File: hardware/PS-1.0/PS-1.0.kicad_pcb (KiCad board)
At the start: 2 copper layers, 98.4 x 199.4 mm, 50 parts, among them J5 Conn_01x04, J8 Conn_01x03, J9 Conn_01x03, K1 RAYEX-L90, K2 RAYEX-L90, Q1 IRFPE50, Q2 IRFPE50, Q3 IRFPE50, U1 TC4422

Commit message: deleted:    hardware/MSD-1.0/MSD-1.0-backups/MSD-1.0-2025-03-24_113503.zip 	new file:   hardware/MSD-1.0/MSD-1.0-backups/MSD-1.0-2025-04-14_090414.zip 	new file:   hardware/MSD-2.0/MSD-2.0-backups/MSD-2.0-2025-04-14_085637.zip 	deleted:    hardware/PS-1.0/PS-1.0-backups/PS-1.0-2025-04-11_100523.zip 	new file:   hardware/PS-1.0/PS-1.0-backups/PS-1.0-2025-04-14_085622.zip 	modified:   hardware/PS-1.0/PS-1.0.kicad_pcb 	deleted:    hardware/PS-1.0/_autosave-PS-1.0.kicad_pcb 	renamed:    hardware/PS-1.0/~PS-1.0.kicad_sch.lck -> hardware/REM-3.0/~REM-3.0.kicad_pcb.lck 	renamed:    hardware/PS-1.0/~_autosave-PS-1.0.kicad_pcb.lck -> hardware/REM-3.0/~REM-3.0.kicad_sch.lck 	modified:   pic/.DS_Store 	new file:   pic/REM/REM XF.png 	new file:   pic/REM/REM-1kohm.png 	new file:   pic/REM/REM-200ohm.png 	new file:   pic/REM/REM-5ohm.png 	new file:   pic/REM/REM-highZ.png
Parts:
- U3: footprint Custom:ESU-REM-3.0 -> Custom:ESU-MSD-1.0
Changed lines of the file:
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@@
 		)
 	)
-	(footprint "Custom:ESU-REM-3.0"
+	(footprint "Custom:ESU-MSD-1.0"
 		(layer "F.Cu")
 		(at 134.62 130.175)
@@
 			)
 		)
-		(property "Footprint" "Custom:ESU-REM-3.0"
+		(property "Footprint" "Custom:ESU-MSD-1.0"
 			(at -9.525 4.1275 0)
 			(unlocked yes)
@@
 			(remove_unused_layers no)
 		)
-		(model "${KIPRJMOD}/REM-3.0.step"
+		(model "/Users/margabudi/Documents/hardware/ESU/hardware/MSD-1.0/MSD-1.0.step"
 			(offset
 				(xyz 1.6 0 0)

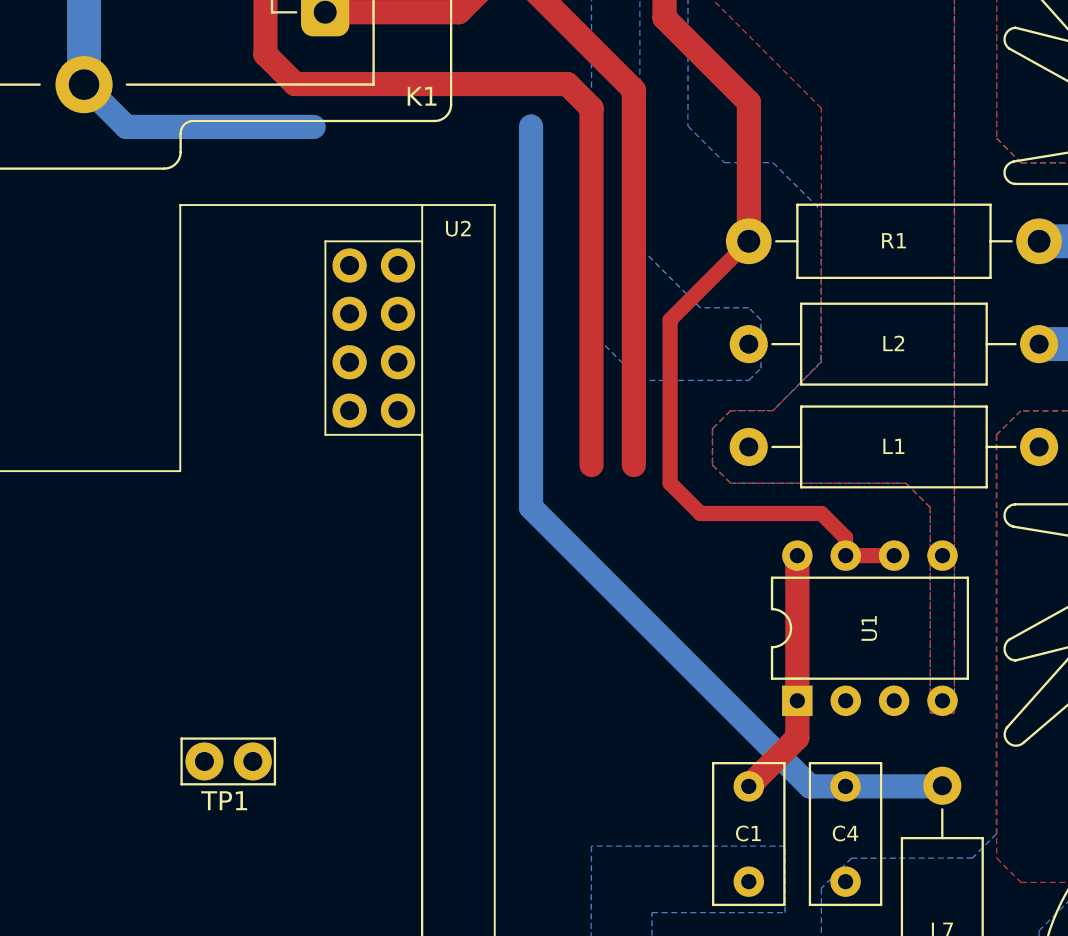
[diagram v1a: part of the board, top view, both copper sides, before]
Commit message: new file:   hardware/Gain/Gain-B_Cu.gbr 	new file:   hardware/Gain/Gain-B_Mask.gbr 	new file:   hardware/Gain/Gain-B_Paste.gbr 	new file:   hardware/Gain/Gain-B_Silkscreen.gbr 	new file:   hardware/Gain/Gain-Edge_Cuts.gbr 	new file:   hardware/Gain/Gain-F_Cu.gbr 	new file:   hardware/Gain/Gain-F_Mask.gbr 	new file:   hardware/Gain/Gain-F_Paste.gbr 	new file:   hardware/Gain/Gain-F_Silkscreen.gbr 	new file:   hardware/Gain/Gain-NPTH.drl 	new file:   hardware/Gain/Gain-PTH.drl 	new file:   hardware/Gain/Gain-backups/Gain-2025-04-14_115147.zip 	new file:   hardware/Gain/Gain-backups/Gain-2025-04-14_121847.zip 	new file:   hardware/Gain/Gain-backups/Gain-2025-04-14_133755.zip 	new file:   hardware/Gain/Gain-backups/Gain-2025-04-14_141907.zip 	new file:   hardware/Gain/Gain-backups/Gain-2025-04-14_162042.zip 	new file:   hardware/Gain/Gain-backups/Gain-2025-04-14_163456.zip 	new file:   hardware/Gain/Gain-job.gbrjob 	new file:   hardware/Gain/Gain.kicad_pcb 	new file:   hardware/Gain/Gain.kicad_prl 	new file:   hardware/Gain/Gain.kicad_pro 	new file:   hardware/Gain/Gain.kicad_sch 	new file:   hardware/Gain/Gain.step 	new file:   hardware/Gain/REM-2.0 BoM.csv 	new file:   hardware/Gain/REM-2.0-backups/REM-2.0-2025-03-05_160217.zip 	new file:   hardware/Gain/REM-2.0-backups/REM-2.0-2025-03-06_081735.zip 	new file:   hardware/Gain/REM-2.0-backups/REM-2.0-2025-03-17_111724.zip 	new file:   hardware/Gain/REM-2.0-backups/REM-2.0-2025-03-17_135033.zip 	new file:   hardware/Gain/REM-2.0-backups/REM-2.0-2025-03-18_104019.zip 	new file:   hardware/Gain/REM-2.0-backups/REM-2.0-2025-03-18_141720.zip 	new file:   hardware/Gain/REM-2.0-backups/REM-2.0-2025-03-18_202240.zip 	new file:   hardware/Gain/REM-2.0-backups/REM-2.0-2025-03-18_203414.zip 	new file:   hardware/Gain/REM-2.0-backups/REM-2.0-2025-03-18_204444.zip 	new file:   hardware/Gain/REM-2.0-backups/REM-2.0-2025-03-24_102406.zip 	new file:   hardware/Gain/REM-2.0-backups/REM-2.0-2025-03-24_103843.zip 	new file:   hardware/Ga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
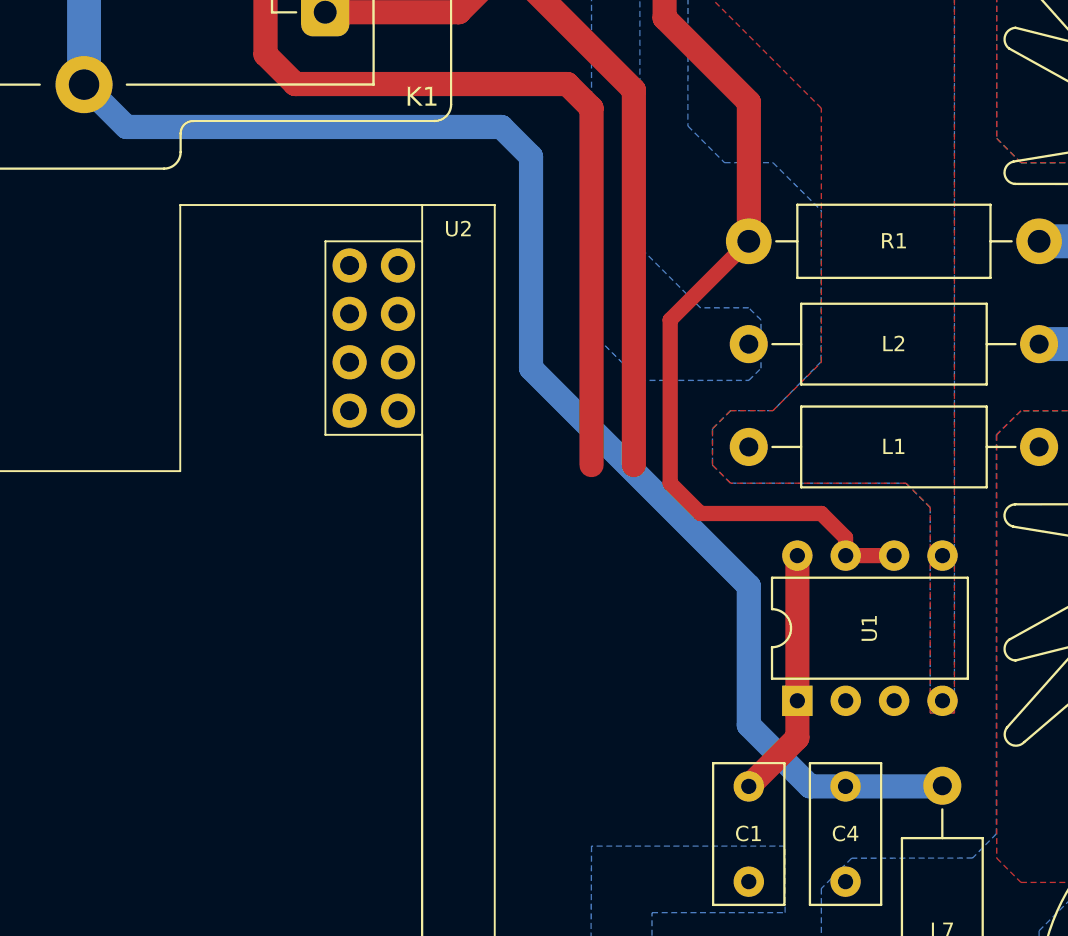
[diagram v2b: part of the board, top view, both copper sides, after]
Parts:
- removed TP1: TestPoint, TestPoint:TestPoint_Bridge_Pitch2.54mm_Drill1.0mm
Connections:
- net Net-(D8-A) renamed /RLY-K
- net Net-(D8-K) renamed /RLY-A
- net Net-(J5-Pin_1) renamed /PWM
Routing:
- net Net-(C4-Pad1): track 110.0 -> 120.4 mm

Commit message: deleted:    hardware/Gain/Gain-backups/Gain-2025-04-14_115147.zip 	new file:   hardware/Gain/Gain-backups/Gain-2025-04-15_120154.zip 	deleted:    hardware/MSD-1.0/MSD-1.0-backups/MSD-1.0-2025-03-24_134332.zip 	deleted:    hardware/MSD-1.0/MSD-1.0-backups/MSD-1.0-2025-03-25_144744.zip 	deleted:    hardware/MSD-1.0/MSD-1.0-backups/MSD-1.0-2025-03-25_145433.zip 	deleted:    hardware/MSD-1.0/MSD-1.0-backups/MSD-1.0-2025-03-25_150210.zip 	deleted:    hardware/MSD-1.0/MSD-1.0-backups/MSD-1.0-2025-03-25_150818.zip 	new file:   hardware/MSD-1.0/MSD-1.0-backups/MSD-1.0-2025-04-16_142822.zip 	new file:   hardware/MSD-1.0/MSD-1.0-backups/MSD-1.0-2025-04-16_143722.zip 	new file:   hardware/MSD-1.0/MSD-1.0-backups/MSD-1.0-2025-04-16_145208.zip 	new file:   hardware/MSD-1.0/MSD-1.0-backups/MSD-1.0-2025-04-16_150237.zip 	new file:   hardware/MSD-1.0/MSD-1.0-backups/MSD-1.0-2025-04-16_150829.zip 	modified:   hardware/MSD-1.0/MSD-1.0.kicad_pcb 	modified:   hardware/MSD-1.0/MSD-1.0.kicad_sch 	modified:   hardware/MSD-1.0/MSD-1.0.step 	new file:   hardware/MSD-2.0/MSD-2.0-backups/MSD-2.0-2025-04-16_090248.zip 	deleted:    hardware/PS-1.0/PS-1.0-backups/PS-1.0-2025-03-18_205016.zip 	deleted:    hardware/PS-1.0/PS-1.0-backups/PS-1.0-2025-03-18_205728.zip 	deleted:    hardware/PS-1.0/PS-1.0-backups/PS-1.0-2025-03-18_211157.zip 	deleted:    hardware/PS-1.0/PS-1.0-backups/PS-1.0-2025-03-18_213933.zip 	deleted:    hardware/PS-1.0/PS-1.0-backups/PS-1.0-2025-03-19_094557.zip 	deleted:    hardware/PS-1.0/PS-1.0-backups/PS-1.0-2025-03-19_101204.zip 	deleted:    hardware/PS-1.0/PS-1.0-backups/PS-1.0-2025-03-19_102323.zip 	new file:   hardware/PS-1.0/PS-1.0-backups/PS-1.0-2025-04-16_154157.zip 	new file:   hardware/PS-1.0/PS-1.0-backups/PS-1.0-2025-04-16_154838.zip 	new file:   hardware/PS-1.0/PS-1.0-backups/PS-1.0-2025-04-16_155906.zip 	new file:   hardware/PS-1.0/PS-1.0-backups/PS-1.0-2025-04-16_160456.zip 	new file:   hardware/PS-1.0/PS-1.0-backups/PS-1.0-2025-04-16_161300.zip 	new file:   har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
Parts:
- removed HS1, HS2, HS3: Heatsink_Pad, Heatsink:Heatsink_Fischer_SK129-STS_42x25mm_2xDrill2.5mm
- removed HS4, HS5: Heatsink_Pad, Heatsink:Heatsink_Stonecold_HS-132_32x14mm_2xFixation1.5mm
- removed J5: Conn_01x04, Connector_PinHeader_2.54mm:PinHeader_1x04_P2.54mm_Vertical
- added J1: Conn_02x16_Odd_Even, Connector_PinSocket_2.54mm:PinSocket_2x16_P2.54mm_Vertical, F.Cu at (182.2, 186.7)
- added J2: Conn_01x05, Connector_Molex:Molex_KK-396_5273-05A_1x05_P3.96mm_Vertical_2, F.Cu at (125.8, 197.8)
- added J3: Conn_01x05, Connector_Molex:Molex_KK-396_5273-05A_1x05_P3.96mm_Vertical_2, F.Cu at (125.7, 173.4)
- U3: footprint Custom:ESU-MSD-1.0 -> Custom:ESU-REM-3.0
- moved CON-01 44.7 mm to (209.6, 179.1), turned to -90 degrees
- moved R5 44.7 mm to (189.9, 152.7), turned to -90 degrees
- moved H1 44.1 mm to (214.3, 35.2)
- moved U3 27.3 mm to (161.9, 128.9)
- moved U2 17.8 mm to (144.8, 128.9)
- moved C1 17.3 mm to (178.4, 143.5), turned to 90 degrees
- moved C2 11.4 mm to (201.0, 160.3)
- moved U1 11.4 mm to (182.2, 144.8)
- moved Q1 11.4 mm to (207.0, 121.9)
- moved D7 10.3 mm to (179.7, 179.1), turned to 0 degrees
- moved D1 10.2 mm to (200.7, 127.3)
- moved D3 10.2 mm to (200.7, 51.1)
- moved C3 10.2 mm to (178.4, 167.9)
- moved C4 10.2 mm to (178.4, 152.8)
- moved R1 10.2 mm to (194.9, 121.9)
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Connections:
- D8 pad 1: /RLY-A -> /RLY-K
- D8 pad 2: /RLY-K -> /RLY-A
- D9 pad 1: /RLY-A -> /RLY-K
- D9 pad 2: /RLY-K -> /RLY-A
- K1 pad A1: /RLY-K -> /RLY-A
- K1 pad A2: /RLY-A -> /RLY-K
- K2 pad A1: /RLY-K -> /RLY-A
- K2 pad A2: /RLY-A -> /RLY-K
- U2 pad 1: (no net) -> Net-(J1-Pin_10)
- U2 pad 2: (no net) -> Net-(J1-Pin_12)
- U2 pad 4: (no net) -> Net-(J1-Pin_18)
- U2 pad 5: (no net) -> Net-(J2-Pin_1)
- U2 pad 6: (no net) -> Net-(J2-Pin_3)
- U2 pad 7: (no net) -> Net-(J2-Pin_5)
- U3 pad 1: (no net) -> Net-(J1-Pin_10)
- U3 pad 2: (no net) -> Net-(J1-Pin_12)
- U3 pad 3: (no net) -> Net-(J1-Pin_14)
- U3 pad 4: (no net) -> Net-(J1-Pin_16)
- U3 pad 5: (no net) -> Net-(J3-Pin_1)
- U3 pad 6: (no net) -> Net-(J3-Pin_3)
- U3 pad 7: (no net) -> Net-(J3-Pin_5)
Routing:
- net Net-(J1-Pin_10): track 0.00 -> 96.1 mm
- net Net-(J1-Pin_12): track 0.00 -> 95.5 mm
- net Net-(J1-Pin_18): track 0.00 -> 92.8 mm
- net Net-(J1-Pin_14): track 0.00 -> 78.0 mm
- net Net-(J1-Pin_16): track 0.00 -> 76.9 mm
- net /RLY-K: track 80.0 -> 154.7 mm
- net Net-(J3-Pin_1): track 0.00 -> 61.1 mm
- net Net-(J3-Pin_3): track 0.00 -> 59.3 mm
- net Net-(J3-Pin_5): track 0.00 -> 56.4 mm
- net /PWM: track 0.00 -> 55.5 mm
- net VDD: track 13.2 -> 67.2 mm
- net /RLY-A: track 101.4 -> 131.8 mm
- net Net-(J2-Pin_1): track 0.00 -> 20.0 mm
- net Net-(J2-Pin_3): track 0.00 -> 18.9 mm
- net Net-(J2-Pin_5): track 0.00 -> 17.7 mm
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- added copper zone on F.Cu, net Net-(D7-K)
- added copper zone on F.Cu, net VS
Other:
- board text added: "0"
- board text added: "38.1"
